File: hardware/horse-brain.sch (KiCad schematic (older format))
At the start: 28 parts, among them P1 M200, P2 Power in, Q1 lu024, Q2 BC547, Q3 2N7000, Q4 2N7000, Q5 2N7000

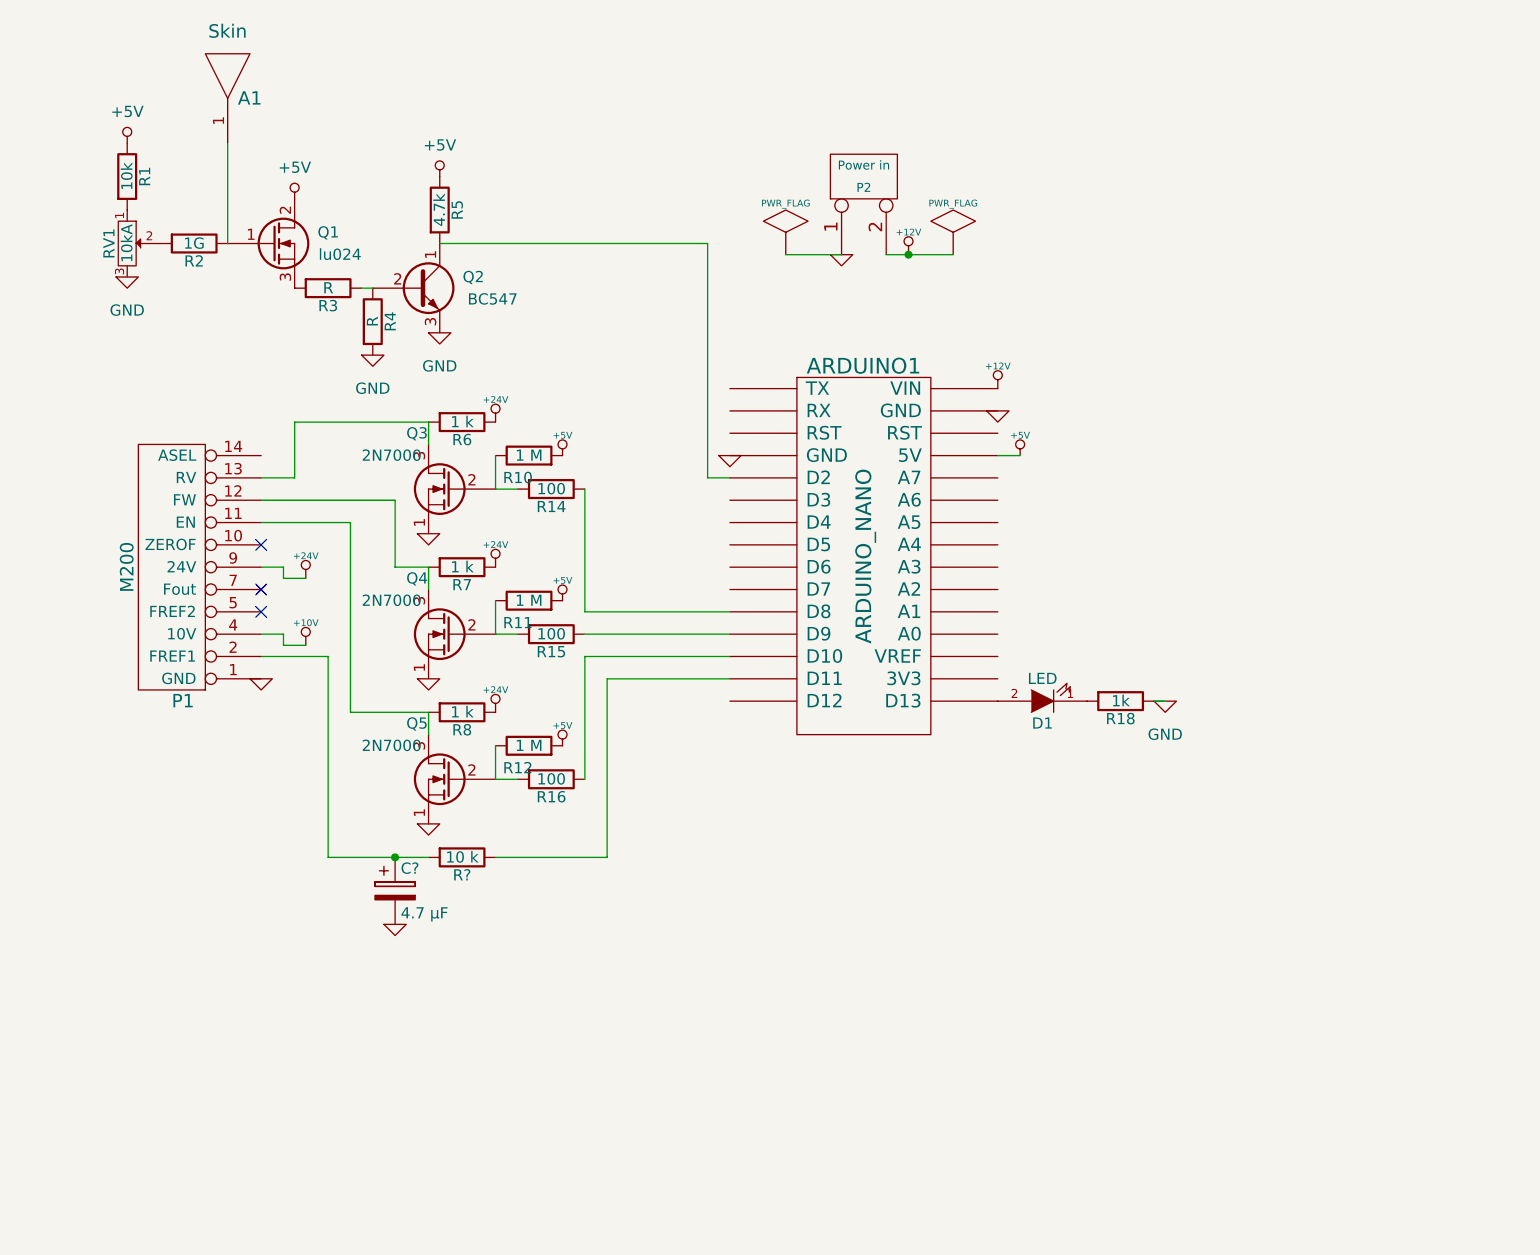
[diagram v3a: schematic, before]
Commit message: Update 4 channel skin, plus hardware of distance sight
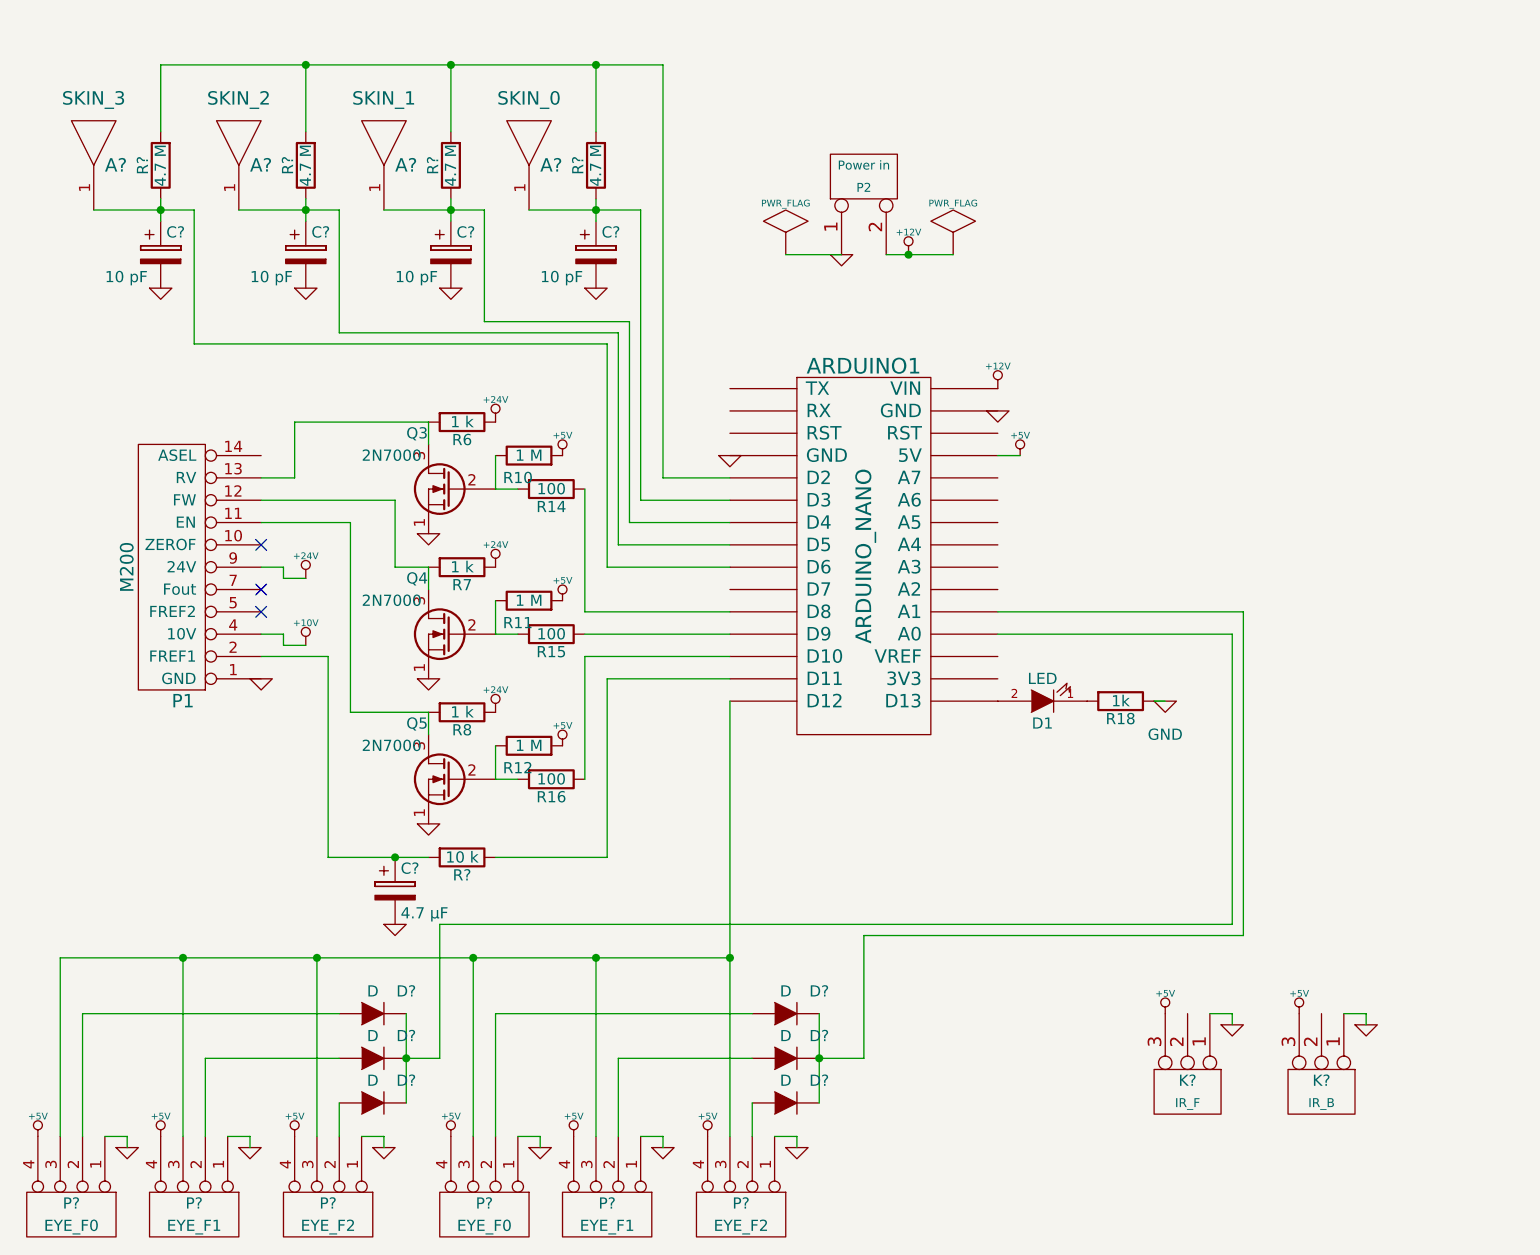
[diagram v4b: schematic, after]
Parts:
- removed A1: Skin, symbol ANTENNA
- removed Q1: lu024, symbol Q_NMOS_GDS
- removed Q2: BC547, symbol Q_NPN_CBE
- removed R1: 10k, symbol R
- removed R2: 1G, symbol R
- removed R3, R4: R, symbol R
- removed R5: 4.7k, symbol R
- removed RV1: 10kA, symbol POT
- added A?: SKIN_3, symbol ANTENNA
- added A?: SKIN_2, symbol ANTENNA
- added A?: SKIN_0, symbol ANTENNA
- added A?: SKIN_1, symbol ANTENNA
- added C? (x4): 10 pF, symbol CP
- added D? (x6): D, symbol D
- added K?: IR_F, symbol CONN_3
- added K?: IR_B, symbol CONN_3
- added P? (x2): EYE_F0, symbol CONN_4
- added P? (x2): EYE_F1, symbol CONN_4
- added P? (x2): EYE_F2, symbol CONN_4
- added R? (x4): 4.7 M, symbol R
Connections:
- net +5V: now also K?.3 (P3), K?.3 (P3), P?.4 (P4), P?.4 (P4), P?.4 (P4), P?.4 (P4), P?.4 (P4), P?.4 (P4)
- net GND: now also C?.2, C?.2, C?.2, C?.2, K?.1 (P1), K?.1 (P1), P?.1 (P1), P?.1 (P1), P?.1 (P1), P?.1 (P1), P?.1 (P1), P?.1 (P1)
- net at ARDUINO1.15 (D12): now also P?.3 (P3), P?.3 (P3), P?.3 (P3), P?.3 (P3), P?.3 (P3), P?.3 (P3)
- net at ARDUINO1.19 (A0): now also D?.1 (K), D?.1 (K), D?.1 (K)
- net at ARDUINO1.20 (A1): now also D?.1 (K), D?.1 (K), D?.1 (K)
- net at ARDUINO1.5 (D2): now also R?.2, R?.2, R?.2, R?.2
- net at ARDUINO1.6 (D3): now also A?.1, C?.1, R?.1
- net at ARDUINO1.7 (D4): now also A?.1, C?.1, R?.1
- net at ARDUINO1.8 (D5): now also A?.1, C?.1, R?.1
- net at ARDUINO1.9 (D6): now also A?.1, C?.1, R?.1
- new net: D?.2 (A), P?.2 (P2) (x6)

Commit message: Fixes to sight
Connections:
- net at ARDUINO1.21 (A2): now also K?.2 (PM)
- net at ARDUINO1.22 (A3): now also K?.2 (PM)
- net at D?.2 (A): now also ARDUINO1.19 (A0), D?.2 (A), D?.2 (A); no longer P?.2 (P2)
- net at P?.2 (P2): now also D?.1 (K); no longer D?.2 (A) (x4)
- net at D?.2 (A): now also ARDUINO1.20 (A1), D?.2 (A), D?.2 (A); no longer P?.2 (P2)
- new net: D?.1 (K), P?.2 (P2) (x2)
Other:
- moved on the sheet: K?
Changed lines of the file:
@@
 F 3 "" H 4500 5900 50  0000 C CNN
 	1    4500 5900
-	-1   0    0    1
+	1    0    0    -1
 $EndComp
 $Comp
@@
 F 3 "" H 4500 6100 50  0000 C CNN
 	1    4500 6100
-	-1   0    0    1
+	1    0    0    -1
 $EndComp
 $Comp
@@
 F 3 "" H 4500 6300 50  0000 C CNN
 	1    4500 6300
-	-1   0    0    1
+	1    0    0    -1
 $EndComp
 $Comp
 L CONN_3 K?
 U 1 1 58485662
-P 8150 6250
-F 0 "K?" V 8100 6250 50  0000 C CNN
-F 1 "IR_F" V 8200 6250 40  0000 C CNN
-F 2 "" H 8150 6250 60  0001 C CNN
-F 3 "" H 8150 6250 60  0001 C CNN
-	1    8150 6250
+P 8800 4550
+F 0 "K?" V 8750 4550 50  0000 C CNN
+F 1 "IR_F" V 8850 4550 40  0000 C CNN
+F 2 "" H 8800 4550 60  0001 C CNN
+F 3 "" H 8800 4550 60  0001 C CNN
+	1    8800 4550
 	0    1    1    0
 $EndComp
@@
 L +5V #PWR?
 U 1 1 58485701
-P 8050 5900
-F 0 "#PWR?" H 8050 5990 20  0001 C CNN
-F 1 "+5V" H 8050 5990 30  0000 C CNN
-F 2 "" H 8050 5900 60  0001 C CNN
-F 3 "" H 8050 5900 60  0001 C CNN
-	1    8050 5900
+P 8700 4200
+F 0 "#PWR?" H 8700 4290 20  0001 C CNN
+F 1 "+5V" H 8700 4290 30  0000 C CNN
+F 2 "" H 8700 4200 60  0001 C CNN
+F 3 "" H 8700 4200 60  0001 C CNN
+	1    8700 4200
 	1    0    0    -1
 $EndComp
@@
 L GND #PWR?
 U 1 1 58485755
-P 8350 5950
-F 0 "#PWR?" H 8350 5950 30  0001 C CNN
-F 1 "GND" H 8350 5880 30  0001 C CNN
-F 2 "" H 8350 5950 60  0001 C CNN
-F 3 "" H 8350 5950 60  0001 C CNN
-	1    8350 5950
+P 9000 4250
+F 0 "#PWR?" H 9000 4250 30  0001 C CNN
+F 1 "GND" H 9000 4180 30  0001 C CNN
+F 2 "" H 9000 4250 60  0001 C CNN
+F 3 "" H 9000 4250 60  0001 C CNN
+	1    9000 4250
 	1    0    0    -1
 $EndComp
@@
 L CONN_3 K?
 U 1 1 58485C6A
-P 8750 6250
-F 0 "K?" V 8700 6250 50  0000 C CNN
-F 1 "IR_B" V 8800 6250 40  0000 C CNN
-F 2 "" H 8750 6250 60  0001 C CNN
-F 3 "" H 8750 6250 60  0001 C CNN
-	1    8750 6250
+P 9400 4550
+F 0 "K?" V 9350 4550 50  0000 C CNN
+F 1 "IR_B" V 9450 4550 40  0000 C CNN
+F 2 "" H 9400 4550 60  0001 C CNN
+F 3 "" H 9400 4550 60  0001 C CNN
+	1    9400 4550
 	0    1    1    0
 $EndComp
@@
 L +5V #PWR?
 U 1 1 58485C70
-P 8650 5900
-F 0 "#PWR?" H 8650 5990 20  0001 C CNN
-F 1 "+5V" H 8650 5990 30  0000 C CNN
-F 2 "" H 8650 5900 60  0001 C CNN
-F 3 "" H 8650 5900 60  0001 C CNN
-	1    8650 5900
+P 9300 4200
+F 0 "#PWR?" H 9300 4290 20  0001 C CNN
+F 1 "+5V" H 9300 4290 30  0000 C CNN
+F 2 "" H 9300 4200 60  0001 C CNN
+F 3 "" H 9300 4200 60  0001 C CNN
+	1    9300 4200
 	1    0    0    -1
 $EndComp
@@
 L GND #PWR?
 U 1 1 58485C76
-P 8950 5950
-F 0 "#PWR?" H 8950 5950 30  0001 C CNN
-F 1 "GND" H 8950 5880 30  0001 C CNN
-F 2 "" H 8950 5950 60  0001 C CNN
-F 3 "" H 8950 5950 60  0001 C CNN
-	1    8950 5950
+P 9600 4250
+F 0 "#PWR?" H 9600 4250 30  0001 C CNN
+F 1 "GND" H 9600 4180 30  0001 C CNN
+F 2 "" H 9600 4250 60  0001 C CNN
+F 3 "" H 9600 4250 60  0001 C CNN
+	1    9600 4250
 	1    0    0    -1
 $EndComp
@@
 	3200 5900 3200 6450
 Wire Wire Line
-	8350 5950 8350 5900
-Wire Wire Line
-	8350 5900 8250 5900
-Wire Wire Line
-	8950 5950 8950 5900
-Wire Wire Line
-	8950 5900 8850 5900
+	9000 4250 9000 4200
+Wire Wire Line
+	9000 4200 8900 4200
+Wire Wire Line
+	9600 4250 9600 4200
+Wire Wire Line
+	9600 4200 9500 4200
 Wire Wire Line
 	5500 2250 5500 2350
@@
 F 3 "" H 6350 5900 50  0000 C CNN
 	1    6350 5900
-	-1   0    0    1
+	1    0    0    -1
 $EndComp
 $Comp
@@
 F 3 "" H 6350 6100 50  0000 C CNN
 	1    6350 6100
-	-1   0    0    1
+	1    0    0    -1
 $EndComp
 $Comp
@@
 F 3 "" H 6350 6300 50  0000 C CNN
 	1    6350 6300
-	-1   0    0    1
+	1    0    0    -1
 $EndComp
 Wire Wire Line
@@
 Wire Wire Line
 	6700 6100 6500 6100
+Wire Wire Line
+	7300 4000 8800 4000
+Wire Wire Line
+	8800 4000 8800 4200
+Wire Wire Line
+	7300 3900 9400 3900
+Wire Wire Line
+	9400 3900 9400 4200
 $EndSCHEMATC
